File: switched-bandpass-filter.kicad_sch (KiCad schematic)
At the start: 0 parts

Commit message: made a start on schematic, and ERC passes
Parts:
- added J1, J2: SMA, symbol Connector:Conn_Coaxial
- added J10: F3 out through hole, symbol Connector:Conn_01x01_Pin
- added J11: F4 out through hole, symbol Connector:Conn_01x01_Pin
- added J3: F4 in through hole, symbol Connector:Conn_01x01_Pin
- added J4: Conn_01x06_Pin, symbol Connector:Conn_01x06_Pin
- added J5: F3 in through hole, symbol Connector:Conn_01x01_Pin
- added J6: F2 in through hole, symbol Connector:Conn_01x01_Pin
- added J7: F1 in through hole, symbol Connector:Conn_01x01_Pin
- added J8: F1 out through hole, symbol Connector:Conn_01x01_Pin
- added J9: F2 out through hole, symbol Connector:Conn_01x01_Pin
- added U1: FST3253MX, SOIC_253MX_ONS, symbol FST3253MX:FST3253MX
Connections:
- new net +12V: J4.5 (Pin_5)
- new net +5V: U1.16
- new net F1 common: J1.1 (In), U1.7
- new net F1 in: J7.1 (Pin_1), U1.6
- new net F1 out: J8.1 (Pin_1), U1.10
- new net F2 common: J2.1 (In), U1.9
- new net F2 in: J6.1 (Pin_1), U1.5
- new net F2 out: J9.1 (Pin_1), U1.11
- new net F3 in: J5.1 (Pin_1), U1.4
- new net F3 out: J10.1 (Pin_1), U1.12
- new net F4 in: J3.1 (Pin_1), U1.3
- new net F4 out: J11.1 (Pin_1), U1.13
- new net GND: J1.2 (Ext), J2.2 (Ext), J4.4 (Pin_4), U1.1, U1.15, U1.8
- new net P1: J4.1 (Pin_1)
- new net P2: J4.2 (Pin_2)
- new net P3: J4.3 (Pin_3)
- new net S0: U1.14
- new net S1: U1.2
- no-connect marks 0 -> 1
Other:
- added sheet switching circuit (switching-circuit.kicad_sch)
- title: (none) -> switched bandpass filter

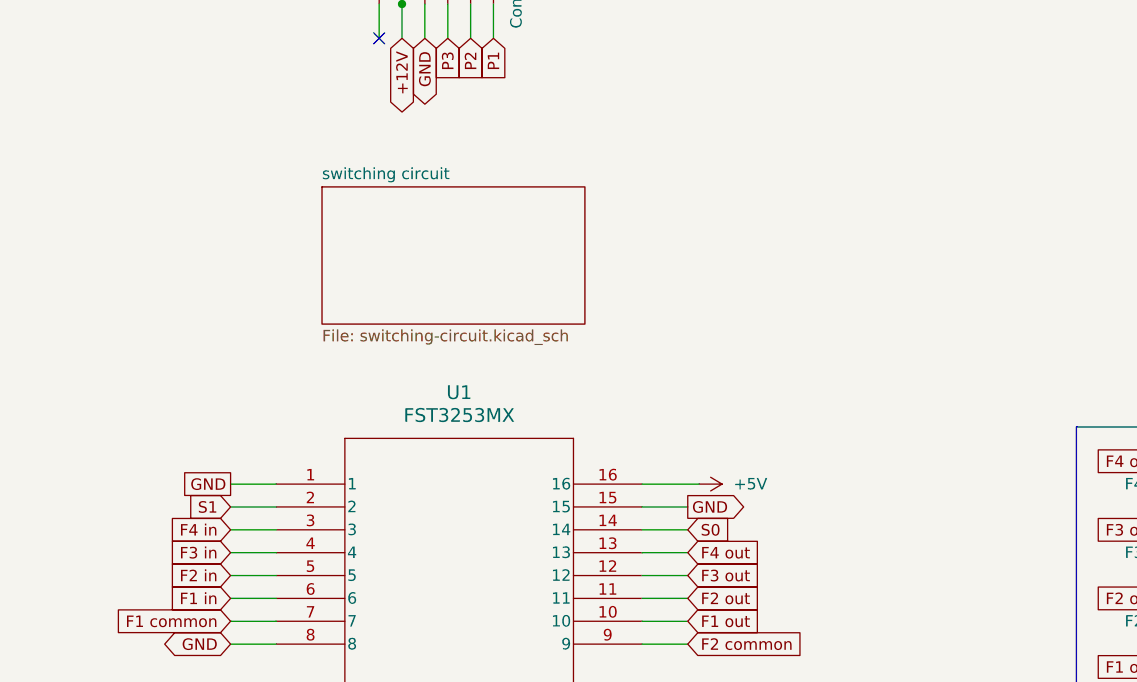
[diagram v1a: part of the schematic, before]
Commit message: added power supply schematic, and deleted the -backups folder
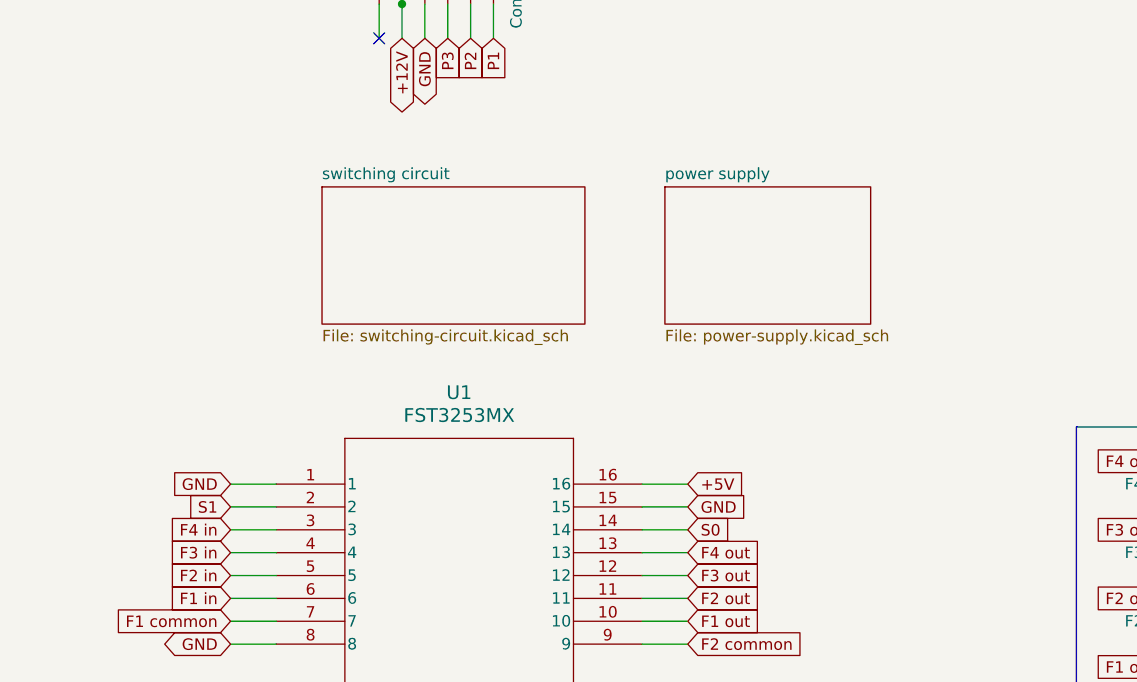
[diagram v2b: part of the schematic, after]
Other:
- added sheet power supply (power-supply.kicad_sch)
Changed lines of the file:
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@@
-    (stroke (width 0) (type default))
-  )
-  (wire (pts (xy 161.29 91.44) (xy 167.64 91.44))
     (stroke (width 0) (type default))
   )
@@
     (stroke (width 0) (type default))
   )
+  (wire (pts (xy 161.29 91.44) (xy 166.37 91.44))
+    (stroke (width 0) (type default))
+  )
   (rectangle (start 209.55 85.09) (end 236.22 118.11)
     (stroke (width 0) (type default))
@@
     )
   )
-  (global_label "GND" (shape passive) (at 115.57 91.44 180) (fields_autoplaced)
-    (effects (font (size 1.27 1.27)) (justify right))
-    (property "Intersheetrefs" "${INTERSHEET_REFS}" (at 110.4004 91.44 0)
+  (global_label "GND" (shape input) (at 115.57 91.44 180) (fields_autoplaced)
+    (effects (font (size 1.27 1.27)) (justify right))
+    (property "Intersheetrefs" "${INTERSHEET_REFS}" (at 109.4479 91.44 0)
       (effects (font (size 1.27 1.27)) (justify right) hide)
     )
@@
     )
   )
+  (global_label "+5V" (shape input) (at 166.37 91.44 0) (fields_autoplaced)
+    (effects (font (size 1.27 1.27)) (justify left))
+    (property "Intersheetrefs" "${INTERSHEET_REFS}" (at 172.4921 91.44 0)
+      (effects (font (size 1.27 1.27)) (justify left) hide)
+    )
+  )
   (global_label "F2 out" (shape input) (at 219.71 104.14 180) (fields_autoplaced)
     (effects (font (size 1.27 1.27)) (justify right))
@@
     )
   )
-  (global_label "GND" (shape output) (at 166.37 93.98 0) (fields_autoplaced)
+  (global_label "GND" (shape input) (at 166.37 93.98 0) (fields_autoplaced)
     (effects (font (size 1.27 1.27)) (justify left))
     (property "Intersheetrefs" "${INTERSHEET_REFS}" (at 172.4921 93.98 0)
@@
         (path "/05f50450-de9a-44de-96d4-4a146d783d83/d4245743-3101-4aa9-985f-bdd1e5cf8eb9"
           (reference "#FLG08") (unit 1)
-        )
-      )
-    )
-  )
-  (symbol (lib_id "power:+5V") (at 167.64 91.44 270) (unit 1)
-    (in_bom yes) (on_board yes) (dnp no) (fields_autoplaced)
-    (property "Reference" "#PWR04" (at 163.83 91.44 0)
-      (effects (font (size 1.27 1.27)) hide)
-    )
-    (property "Value" "+5V" (at 171.45 91.44 90)
-      (effects (font (size 1.27 1.27)) (justify left))
-    )
-    (property "Footprint" "" (at 167.64 91.44 0)
-      (effects (font (size 1.27 1.27)) hide)
-    )
-    (property "Datasheet" "" (at 167.64 91.44 0)
-      (effects (font (size 1.27 1.27)) hide)
-    )
-    (pin "1")
-    (instances
-      (project "switched-bandpass-filter"
-        (path "/05f50450-de9a-44de-96d4-4a146d783d83"
-          (reference "#PWR04") (unit 1)
         )
       )
@@
       )
     )
+  )
+  (sheet (at 163.83 58.42) (size 22.86 15.24) (fields_autoplaced)
+    (stroke (width 0.1524) (type solid))
+    (fill (color 0 0 0 0.0000))
+    (property "Sheetname" "power supply" (at 163.83 57.7084 0)
+      (effects (font (size 1.27 1.27)) (justify left bottom))
+    )
+    (property "Sheetfile" "power-supply.kicad_sch" (at 163.83 74.2446 0)
+      (effects (font (size 1.27 1.27)) (justify left top))
+    )
+    (instances
+      (project "switched-bandpass-filter"
+        (path "/05f50450-de9a-44de-96d4-4a146d783d83" (page "3"))
+      )
+    )

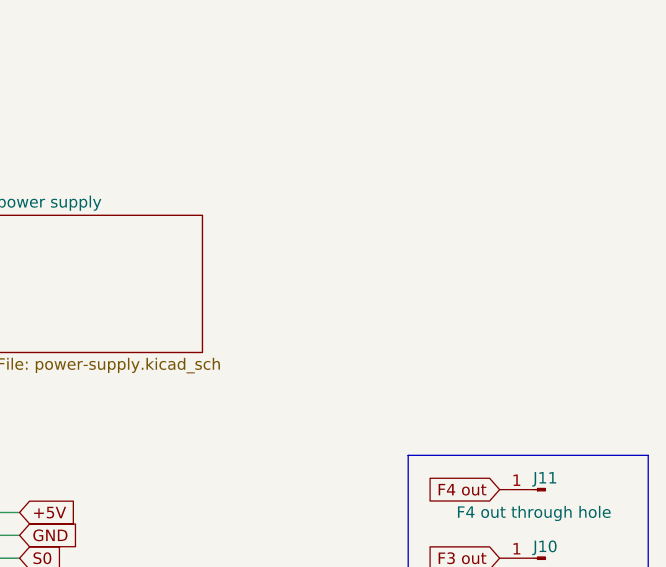
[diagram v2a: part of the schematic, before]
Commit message: added filter ckt, passes ERC, bumped to v0.2, ready for board layout
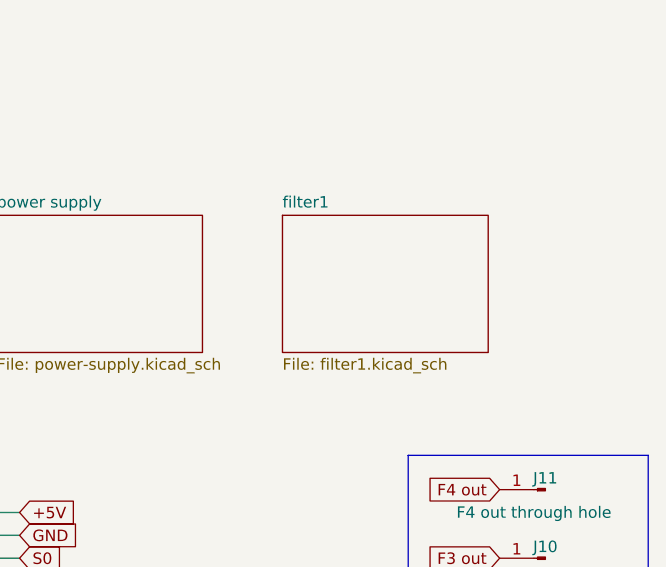
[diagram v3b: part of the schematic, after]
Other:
- added sheet filter1 (filter1.kicad_sch)
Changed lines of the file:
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@@
     (title "switched bandpass filter")
     (date "2023-07-20")
-    (rev "v0.1")
+    (rev "v0.2")
+    (comment 1 "Copyright © 2023 WA7GIL")
   )
   (junction (at 134.62 38.1) (diameter 0) (color 0 0 0 0)
@@
       )
     )
+  )
+  (sheet (at 195.58 58.42) (size 22.86 15.24) (fields_autoplaced)
+    (stroke (width 0.1524) (type solid))
+    (fill (color 0 0 0 0.0000))
+    (property "Sheetname" "filter1" (at 195.58 57.7084 0)
+      (effects (font (size 1.27 1.27)) (justify left bottom))
+    )
+    (property "Sheetfile" "filter1.kicad_sch" (at 195.58 74.2446 0)
+      (effects (font (size 1.27 1.27)) (justify left top))
+    )
+    (instances
+      (project "switched-bandpass-filter"
+        (path "/05f50450-de9a-44de-96d4-4a146d783d83" (page "4"))
+      )
+    )

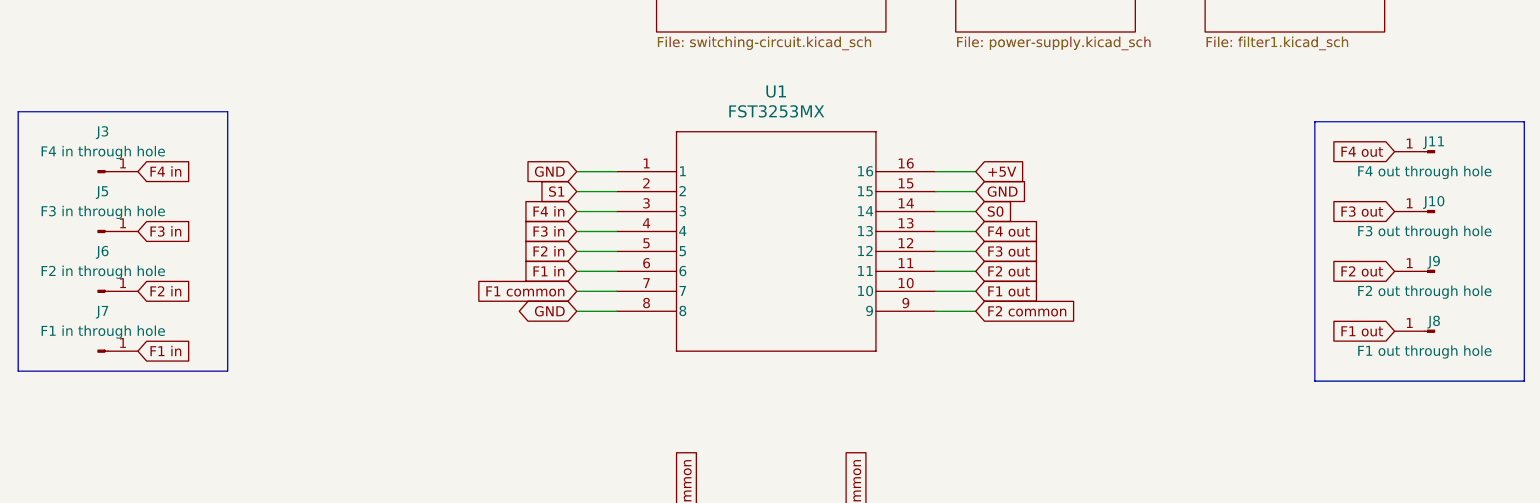
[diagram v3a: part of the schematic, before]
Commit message: v0.2 passes ERC & DRC except for no solder mask between pads on SOT89
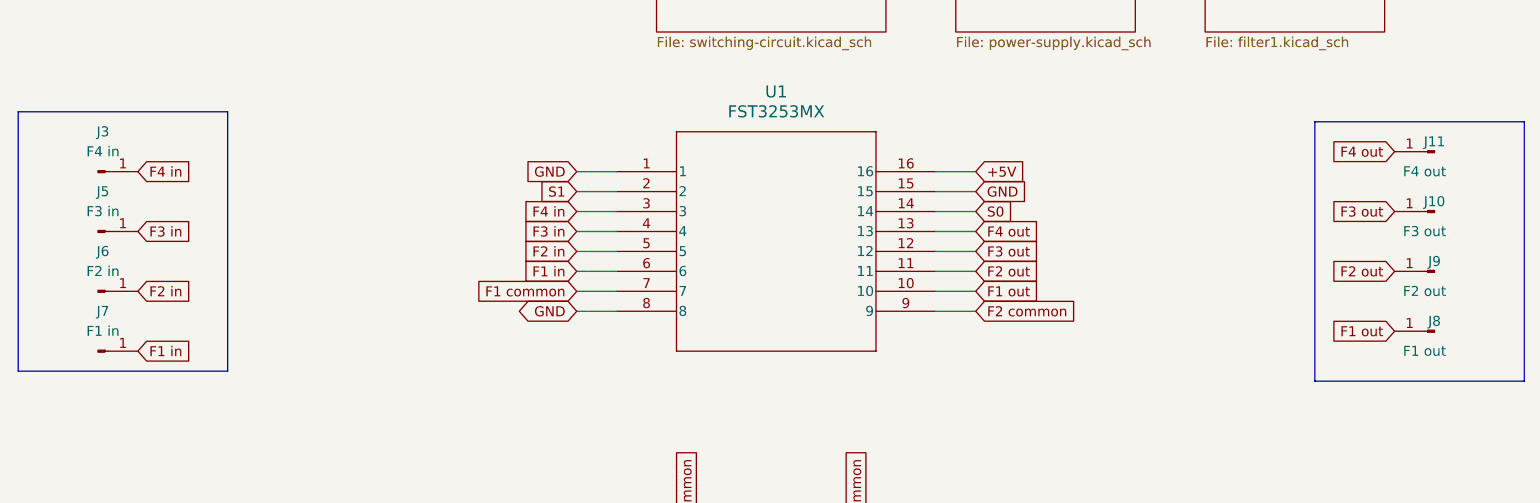
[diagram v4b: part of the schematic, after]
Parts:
- J1, J2: footprint (none) -> Connector_Coaxial:SMA_Amphenol_901-144_Vertical
- J10: value F3 out through hole -> F3 out; footprint (none) -> Connector_PinHeader_2.54mm:PinHeader_1x01_P2.54mm_Vertical
- J11: value F4 out through hole -> F4 out; footprint (none) -> Connector_PinHeader_2.54mm:PinHeader_1x01_P2.54mm_Vertical
- J3: value F4 in through hole -> F4 in; footprint (none) -> Connector_PinHeader_2.54mm:PinHeader_1x01_P2.54mm_Vertical
- J4: footprint (none) -> Connector_PinHeader_2.54mm:PinHeader_1x06_P2.54mm_Vertical
- J5: value F3 in through hole -> F3 in; footprint (none) -> Connector_PinHeader_2.54mm:PinHeader_1x01_P2.54mm_Vertical
- J6: value F2 in through hole -> F2 in; footprint (none) -> Connector_PinHeader_2.54mm:PinHeader_1x01_P2.54mm_Vertical
- J7: value F1 in through hole -> F1 in; footprint (none) -> Connector_PinHeader_2.54mm:PinHeader_1x01_P2.54mm_Vertical
- J8: value F1 out through hole -> F1 out; footprint (none) -> Connector_PinHeader_2.54mm:PinHeader_1x01_P2.54mm_Vertical
- J9: value F2 out through hole -> F2 out; footprint (none) -> Connector_PinHeader_2.54mm:PinHeader_1x01_P2.54mm_Vertical
- U1: footprint SOIC_253MX_ONS -> Package_SO:SOIC-16_3.9x9.9mm_P1.27mm
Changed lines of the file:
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@@
       (effects (font (size 1.27 1.27)))
     )
-    (property "Value" "F4 out through hole" (at 223.52 91.44 0)
-      (effects (font (size 1.27 1.27)))
-    )
-    (property "Footprint" "" (at 224.79 88.9 0)
+    (property "Value" "F4 out" (at 223.52 91.44 0)
+      (effects (font (size 1.27 1.27)))
+    )
+    (property "Footprint" "Connector_PinHeader_2.54mm:PinHeader_1x01_P2.54mm_Vertical" (at 224.79 88.9 0)
       (effects (font (size 1.27 1.27)) hide)
     )
@@
       (effects (font (size 1.27 1.27)))
     )
-    (property "Value" "F2 in through hole" (at 55.245 104.14 0)
-      (effects (font (size 1.27 1.27)))
-    )
-    (property "Footprint" "" (at 54.61 106.68 0)
+    (property "Value" "F2 in" (at 55.245 104.14 0)
+      (effects (font (size 1.27 1.27)))
+    )
+    (property "Footprint" "Connector_PinHeader_2.54mm:PinHeader_1x01_P2.54mm_Vertical" (at 54.61 106.68 0)
       (effects (font (size 1.27 1.27)) hide)
     )
@@
       (effects (font (size 1.524 1.524)))
     )
-    (property "Footprint" "SOIC_253MX_ONS" (at 120.65 91.44 0)
+    (property "Footprint" "Package_SO:SOIC-16_3.9x9.9mm_P1.27mm" (at 120.65 91.44 0)
       (effects (font (size 1.27 1.27) italic) hide)
     )
@@
       (effects (font (size 1.27 1.27)))
     )
-    (property "Footprint" "" (at 139.7 33.02 0)
+    (property "Footprint" "Connector_PinHeader_2.54mm:PinHeader_1x06_P2.54mm_Vertical" (at 139.7 33.02 0)
       (effects (font (size 1.27 1.27)) hide)
     )
@@
       (effects (font (size 1.27 1.27)))
     )
-    (property "Value" "F1 in through hole" (at 55.245 111.76 0)
-      (effects (font (size 1.27 1.27)))
-    )
-    (property "Footprint" "" (at 54.61 114.3 0)
+    (property "Value" "F1 in" (at 55.245 111.76 0)
+      (effects (font (size 1.27 1.27)))
+    )
+    (property "Footprint" "Connector_PinHeader_2.54mm:PinHeader_1x01_P2.54mm_Vertical" (at 54.61 114.3 0)
       (effects (font (size 1.27 1.27)) hide)
     )
@@
       (effects (font (size 1.27 1.27)))
     )
-    (property "Value" "F3 out through hole" (at 223.52 99.06 0)
-      (effects (font (size 1.27 1.27)))
-    )
-    (property "Footprint" "" (at 224.79 96.52 0)
+    (property "Value" "F3 out" (at 223.52 99.06 0)
+      (effects (font (size 1.27 1.27)))
+    )
+    (property "Footprint" "Connector_PinHeader_2.54mm:PinHeader_1x01_P2.54mm_Vertical" (at 224.79 96.52 0)
       (effects (font (size 1.27 1.27)) hide)
     )
@@
       (effects (font (size 1.27 1.27)) (justify left))
     )
-    (property "Footprint" "" (at 134.62 144.78 0)
+    (property "Footprint" "Connector_Coaxial:SMA_Amphenol_901-144_Vertical" (at 134.62 144.78 0)
       (effects (font (size 1.27 1.27)) hide)
     )
@@
       (effects (font (size 1.27 1.27)))
     )
-    (property "Value" "F1 out through hole" (at 223.52 114.3 0)
-      (effects (font (size 1.27 1.27)))
-    )
-    (property "Footprint" "" (at 224.79 111.76 0)
+    (property "Value" "F1 out" (at 223.52 114.3 0)
+      (effects (font (size 1.27 1.27)))
+    )
+    (property "Footprint" "Connector_PinHeader_2.54mm:PinHeader_1x01_P2.54mm_Vertical" (at 224.79 111.76 0)
       (effects (font (size 1.27 1.27)) hide)
     )
@@
       (effects (font (size 1.27 1.27)) (justify left))
     )
-    (property "Footprint" "" (at 156.21 144.78 0)
+    (property "Footprint" "Connector_Coaxial:SMA_Amphenol_901-144_Vertical" (at 156.21 144.78 0)
       (effects (font (size 1.27 1.27)) hide)
     )
@@
       (effects (font (size 1.27 1.27)))
     )
-    (property "Value" "F3 in through hole" (at 55.245 96.52 0)
-      (effects (font (size 1.27 1.27)))
-    )
-    (property "Footprint" "" (at 54.61 99.06 0)
+    (property "Value" "F3 in" (at 55.245 96.52 0)
+      (effects (font (size 1.27 1.27)))
+    )
+    (property "Footprint" "Connector_PinHeader_2.54mm:PinHeader_1x01_P2.54mm_Vertical" (at 54.61 99.06 0)
       (effects (font (size 1.27 1.27)) hide)
     )
@@
       (effects (font (size 1.27 1.27)))
     )
-    (property "Value" "F4 in through hole" (at 55.245 88.9 0)
-      (effects (font (size 1.27 1.27)))
-    )
-    (property "Footprint" "" (at 54.61 91.44 0)
+    (property "Value" "F4 in" (at 55.245 88.9 0)
+      (effects (font (size 1.27 1.27)))
+    )
+    (property "Footprint" "Connector_PinHeader_2.54mm:PinHeader_1x01_P2.54mm_Vertical" (at 54.61 91.44 0)
       (effects (font (size 1.27 1.27)) hide)
     )
@@
       (effects (font (size 1.27 1.27)))
     )
-    (property "Value" "F2 out through hole" (at 223.52 106.68 0)
-      (effects (font (size 1.27 1.27)))
-    )
-    (property "Footprint" "" (at 224.79 104.14 0)
-      (effects (font (size 1.27 1.27)) hide)
-    )
+    (property "Value" "F2 out" (at 223.52 106.68 0)
+      (effects (font (size 1.27 1.27)))
+    )
+    (property "Footprint" "Connector_PinHeader_2.54mm:PinHeader_1x01_P2.54mm_Vertical" (at 224.79 104.14 0)
+      (effects (font (size 1.27 1.27)) hide)
+    )
